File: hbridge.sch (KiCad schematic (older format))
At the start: 16 parts, among them M1 Motor_DC_ALT, Q1 VN2222L, Q2 VN2222L, Q3 IRFZ44, Q4 IRFZ44, Q5 IRFZ44, Q6 IRFZ44, U6 ILD74, U7 LT1161CN-PBF

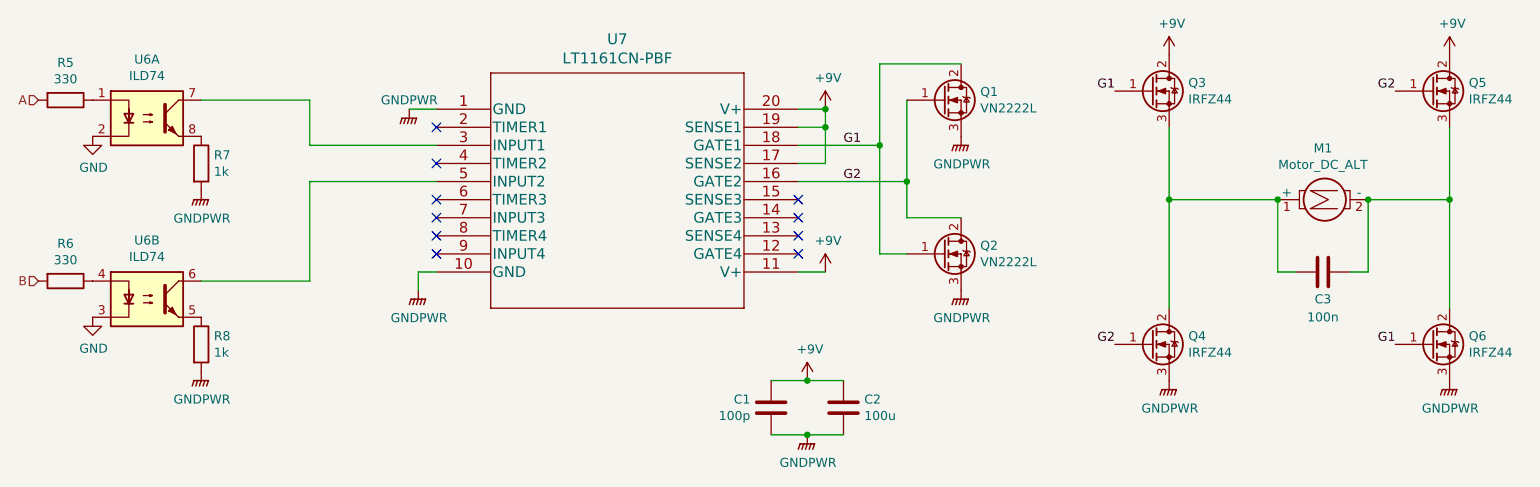
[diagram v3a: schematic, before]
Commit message: Add servos and can brush motor
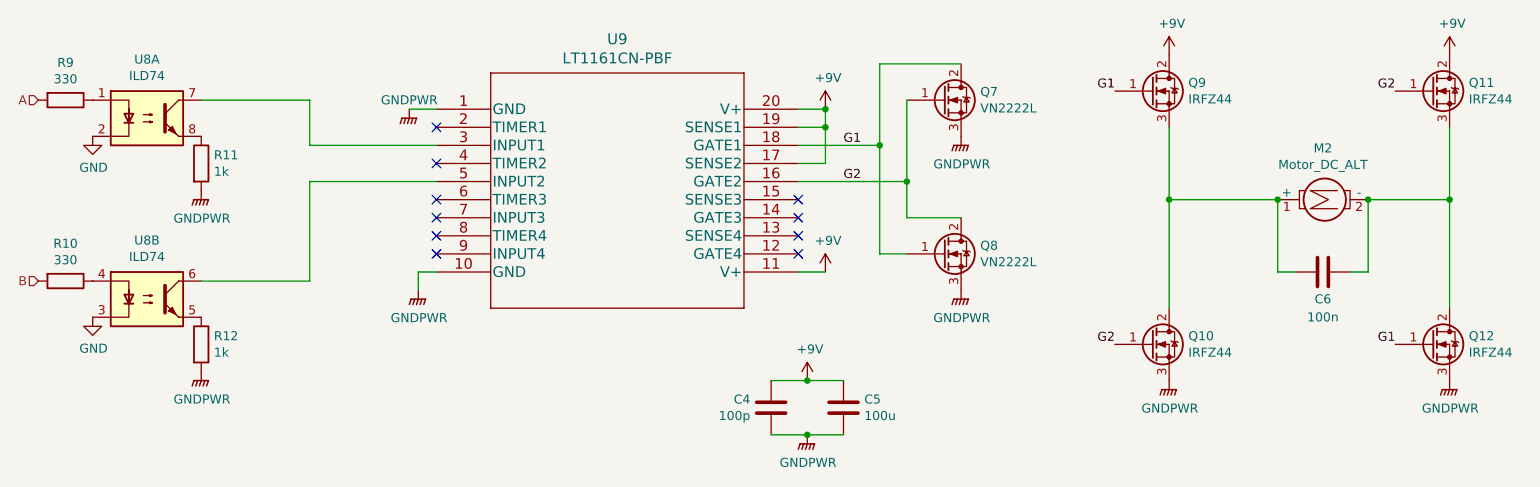
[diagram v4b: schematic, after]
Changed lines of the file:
@@
 AR Path="/5EFA9D4F/5EFAE763" Ref="M1"  Part="1"
 AR Path="/5F04487B/5EFAE763" Ref="M2"  Part="1"
-F 0 "M1" V 8716 3450 50  0000 C CNN
+F 0 "M2" V 8716 3450 50  0000 C CNN
 F 1 "Motor_DC_ALT" V 8807 3450 50  0000 C CNN
 F 2 "" H 9000 3410 50  0001 C CNN
@@
 AR Path="/5EFA9D4F/5EFB4C9B" Ref="U6"  Part="1"
 AR Path="/5F04487B/5EFB4C9B" Ref="U8"  Part="1"
-F 0 "U6" H 2550 3375 50  0000 C CNN
+F 0 "U8" H 2550 3375 50  0000 C CNN
 F 1 "ILD74" H 2550 3284 50  0000 C CNN
 F 2 "" H 2350 2850 50  0001 L CIN
@@
 AR Path="/5EFA9D4F/5EFB57BF" Ref="U6"  Part="2"
 AR Path="/5F04487B/5EFB57BF" Ref="U8"  Part="2"
-F 0 "U6" H 2550 4375 50  0000 C CNN
+F 0 "U8" H 2550 4375 50  0000 C CNN
 F 1 "ILD74" H 2550 4284 50  0000 C CNN
 F 2 "" H 2350 3850 50  0001 L CIN
@@
 AR Path="/5EFA9D4F/5EFB6EDB" Ref="R8"  Part="1"
 AR Path="/5F04487B/5EFB6EDB" Ref="R12"  Part="1"
-F 0 "R8" H 2920 4346 50  0000 L CNN
+F 0 "R12" H 2920 4346 50  0000 L CNN
 F 1 "1k" H 2920 4255 50  0000 L CNN
 F 2 "" V 2780 4300 50  0001 C CNN
@@
 AR Path="/5EFA9D4F/5EFB7506" Ref="R7"  Part="1"
 AR Path="/5F04487B/5EFB7506" Ref="R11"  Part="1"
-F 0 "R7" H 2920 3346 50  0000 L CNN
+F 0 "R11" H 2920 3346 50  0000 L CNN
 F 1 "1k" H 2920 3255 50  0000 L CNN
 F 2 "" V 2780 3300 50  0001 C CNN
@@
 AR Path="/5EFA9D4F/5EFB9D51" Ref="R5"  Part="1"
 AR Path="/5F04487B/5EFB9D51" Ref="R9"  Part="1"
-F 0 "R5" V 1893 2950 50  0000 C CNN
+F 0 "R9" V 1893 2950 50  0000 C CNN
 F 1 "330" V 1984 2950 50  0000 C CNN
 F 2 "" V 2030 2950 50  0001 C CNN
@@
 AR Path="/5EFA9D4F/5EFBA4CA" Ref="R6"  Part="1"
 AR Path="/5F04487B/5EFBA4CA" Ref="R10"  Part="1"
-F 0 "R6" V 1893 3950 50  0000 C CNN
+F 0 "R10" V 1893 3950 50  0000 C CNN
 F 1 "330" V 1984 3950 50  0000 C CNN
 F 2 "" V 2030 3950 50  0001 C CNN
@@
 AR Path="/5EFA9D4F/5EFBBB55" Ref="C1"  Part="1"
 AR Path="/5F04487B/5EFBBB55" Ref="C4"  Part="1"
-F 0 "C1" H 5885 4604 50  0000 R CNN
+F 0 "C4" H 5885 4604 50  0000 R CNN
 F 1 "100p" H 5885 4695 50  0000 R CNN
 F 2 "" H 6038 4500 50  0001 C CNN
@@
 AR Path="/5EFA9D4F/5EFBC147" Ref="C2"  Part="1"
 AR Path="/5F04487B/5EFBC147" Ref="C5"  Part="1"
-F 0 "C2" H 6515 4696 50  0000 L CNN
+F 0 "C5" H 6515 4696 50  0000 L CNN
 F 1 "100u" H 6515 4605 50  0000 L CNN
 F 2 "" H 6438 4500 50  0001 C CNN
@@
 AR Path="/5EFA9D4F/5EFE7548" Ref="Q1"  Part="1"
 AR Path="/5F04487B/5EFE7548" Ref="Q7"  Part="1"
-F 0 "Q1" H 7156 2996 50  0000 L CNN
+F 0 "Q7" H 7156 2996 50  0000 L CNN
 F 1 "VN2222L" H 7156 2905 50  0000 L CNN
 F 2 "" H 7150 3050 50  0001 C CNN
@@
 AR Path="/5EFA9D4F/5EFE9639" Ref="Q2"  Part="1"
 AR Path="/5F04487B/5EFE9639" Ref="Q8"  Part="1"
-F 0 "Q2" H 7156 3846 50  0000 L CNN
+F 0 "Q8" H 7156 3846 50  0000 L CNN
 F 1 "VN2222L" H 7156 3755 50  0000 L CNN
 F 2 "" H 7150 3900 50  0001 C CNN
@@
 AR Path="/5EFA9D4F/5EFE9DB0" Ref="Q3"  Part="1"
 AR Path="/5F04487B/5EFE9DB0" Ref="Q9"  Part="1"
-F 0 "Q3" H 8306 2946 50  0000 L CNN
+F 0 "Q9" H 8306 2946 50  0000 L CNN
 F 1 "IRFZ44" H 8306 2855 50  0000 L CNN
 F 2 "" H 8300 3000 50  0001 C CNN
@@
 AR Path="/5EFA9D4F/5EFEA31E" Ref="Q4"  Part="1"
 AR Path="/5F04487B/5EFEA31E" Ref="Q10"  Part="1"
-F 0 "Q4" H 8306 4346 50  0000 L CNN
+F 0 "Q10" H 8306 4346 50  0000 L CNN
 F 1 "IRFZ44" H 8306 4255 50  0000 L CNN
 F 2 "" H 8300 4400 50  0001 C CNN
@@
 AR Path="/5EFA9D4F/5EFEB4E2" Ref="Q5"  Part="1"
 AR Path="/5F04487B/5EFEB4E2" Ref="Q11"  Part="1"
-F 0 "Q5" H 9856 2946 50  0000 L CNN
+F 0 "Q11" H 9856 2946 50  0000 L CNN
 F 1 "IRFZ44" H 9856 2855 50  0000 L CNN
 F 2 "" H 9850 3000 50  0001 C CNN
@@
 AR Path="/5EFA9D4F/5EFEB900" Ref="Q6"  Part="1"
 AR Path="/5F04487B/5EFEB900" Ref="Q12"  Part="1"
-F 0 "Q6" H 9856 4346 50  0000 L CNN
+F 0 "Q12" H 9856 4346 50  0000 L CNN
 F 1 "IRFZ44" H 9856 4255 50  0000 L CNN
 F 2 "" H 9850 4400 50  0001 C CNN
@@
 AR Path="/5EFA9D4F/5EFAF223" Ref="C3"  Part="1"
 AR Path="/5F04487B/5EFAF223" Ref="C6"  Part="1"
-F 0 "C3" V 9200 3900 50  0000 C CNN
+F 0 "C6" V 9200 3900 50  0000 C CNN
 F 1 "100n" V 9300 3900 50  0000 C CNN
 F 2 "" H 9088 3750 50  0001 C CNN
@@
 AR Path="/5EFA9D4F/5EFCF468" Ref="U7"  Part="1"
 AR Path="/5F04487B/5EFCF468" Ref="U9"  Part="1"
-F 0 "U7" H 5150 3387 60  0000 C CNN
+F 0 "U9" H 5150 3387 60  0000 C CNN
 F 1 "LT1161CN-PBF" H 5150 3281 60  0000 C CNN
 F 2 "PDIP-20_N_LIT" H 5150 3240 60  0001 C CNN

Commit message: Misc minor fixes
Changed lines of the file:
@@
 $Descr A4 11693 8268
 encoding utf-8
-Sheet 2 6
+Sheet 3 6
 Title ""
 Date ""
@@
 AR Path="/5EFA9D4F/5EFAE763" Ref="M1"  Part="1"
 AR Path="/5F04487B/5EFAE763" Ref="M2"  Part="1"
-F 0 "M2" V 8716 3450 50  0000 C CNN
+F 0 "M1" V 8716 3450 50  0000 C CNN
 F 1 "Motor_DC_ALT" V 8807 3450 50  0000 C CNN
 F 2 "" H 9000 3410 50  0001 C CNN
@@
 AR Path="/5EFA9D4F/5EFB4C9B" Ref="U6"  Part="1"
 AR Path="/5F04487B/5EFB4C9B" Ref="U8"  Part="1"
-F 0 "U8" H 2550 3375 50  0000 C CNN
+F 0 "U6" H 2550 3375 50  0000 C CNN
 F 1 "ILD74" H 2550 3284 50  0000 C CNN
 F 2 "" H 2350 2850 50  0001 L CIN
@@
 AR Path="/5EFA9D4F/5EFB57BF" Ref="U6"  Part="2"
 AR Path="/5F04487B/5EFB57BF" Ref="U8"  Part="2"
-F 0 "U8" H 2550 4375 50  0000 C CNN
+F 0 "U6" H 2550 4375 50  0000 C CNN
 F 1 "ILD74" H 2550 4284 50  0000 C CNN
 F 2 "" H 2350 3850 50  0001 L CIN
@@
 AR Path="/5EFA9D4F/5EFB6EDB" Ref="R8"  Part="1"
 AR Path="/5F04487B/5EFB6EDB" Ref="R12"  Part="1"
-F 0 "R12" H 2920 4346 50  0000 L CNN
+F 0 "R8" H 2920 4346 50  0000 L CNN
 F 1 "1k" H 2920 4255 50  0000 L CNN
 F 2 "" V 2780 4300 50  0001 C CNN
@@
 AR Path="/5EFA9D4F/5EFB7506" Ref="R7"  Part="1"
 AR Path="/5F04487B/5EFB7506" Ref="R11"  Part="1"
-F 0 "R11" H 2920 3346 50  0000 L CNN
+F 0 "R7" H 2920 3346 50  0000 L CNN
 F 1 "1k" H 2920 3255 50  0000 L CNN
 F 2 "" V 2780 3300 50  0001 C CNN
@@
 AR Path="/5EFA9D4F/5EFB9D51" Ref="R5"  Part="1"
 AR Path="/5F04487B/5EFB9D51" Ref="R9"  Part="1"
-F 0 "R9" V 1893 2950 50  0000 C CNN
+F 0 "R5" V 1893 2950 50  0000 C CNN
 F 1 "330" V 1984 2950 50  0000 C CNN
 F 2 "" V 2030 2950 50  0001 C CNN
@@
 AR Path="/5EFA9D4F/5EFBA4CA" Ref="R6"  Part="1"
 AR Path="/5F04487B/5EFBA4CA" Ref="R10"  Part="1"
-F 0 "R10" V 1893 3950 50  0000 C CNN
+F 0 "R6" V 1893 3950 50  0000 C CNN
 F 1 "330" V 1984 3950 50  0000 C CNN
 F 2 "" V 2030 3950 50  0001 C CNN
@@
 AR Path="/5EFA9D4F/5EFBBB55" Ref="C1"  Part="1"
 AR Path="/5F04487B/5EFBBB55" Ref="C4"  Part="1"
-F 0 "C4" H 5885 4604 50  0000 R CNN
+F 0 "C1" H 5885 4604 50  0000 R CNN
 F 1 "100p" H 5885 4695 50  0000 R CNN
 F 2 "" H 6038 4500 50  0001 C CNN
@@
 AR Path="/5EFA9D4F/5EFBC147" Ref="C2"  Part="1"
 AR Path="/5F04487B/5EFBC147" Ref="C5"  Part="1"
-F 0 "C5" H 6515 4696 50  0000 L CNN
+F 0 "C2" H 6515 4696 50  0000 L CNN
 F 1 "100u" H 6515 4605 50  0000 L CNN
 F 2 "" H 6438 4500 50  0001 C CNN
@@
 AR Path="/5EFA9D4F/5EFE7548" Ref="Q1"  Part="1"
 AR Path="/5F04487B/5EFE7548" Ref="Q7"  Part="1"
-F 0 "Q7" H 7156 2996 50  0000 L CNN
+F 0 "Q1" H 7156 2996 50  0000 L CNN
 F 1 "VN2222L" H 7156 2905 50  0000 L CNN
 F 2 "" H 7150 3050 50  0001 C CNN
@@
 AR Path="/5EFA9D4F/5EFE9639" Ref="Q2"  Part="1"
 AR Path="/5F04487B/5EFE9639" Ref="Q8"  Part="1"
-F 0 "Q8" H 7156 3846 50  0000 L CNN
+F 0 "Q2" H 7156 3846 50  0000 L CNN
 F 1 "VN2222L" H 7156 3755 50  0000 L CNN
 F 2 "" H 7150 3900 50  0001 C CNN
@@
 AR Path="/5EFA9D4F/5EFE9DB0" Ref="Q3"  Part="1"
 AR Path="/5F04487B/5EFE9DB0" Ref="Q9"  Part="1"
-F 0 "Q9" H 8306 2946 50  0000 L CNN
+F 0 "Q3" H 8306 2946 50  0000 L CNN
 F 1 "IRFZ44" H 8306 2855 50  0000 L CNN
 F 2 "" H 8300 3000 50  0001 C CNN
@@
 AR Path="/5EFA9D4F/5EFEA31E" Ref="Q4"  Part="1"
 AR Path="/5F04487B/5EFEA31E" Ref="Q10"  Part="1"
-F 0 "Q10" H 8306 4346 50  0000 L CNN
+F 0 "Q4" H 8306 4346 50  0000 L CNN
 F 1 "IRFZ44" H 8306 4255 50  0000 L CNN
 F 2 "" H 8300 4400 50  0001 C CNN
@@
 AR Path="/5EFA9D4F/5EFEB4E2" Ref="Q5"  Part="1"
 AR Path="/5F04487B/5EFEB4E2" Ref="Q11"  Part="1"
-F 0 "Q11" H 9856 2946 50  0000 L CNN
+F 0 "Q5" H 9856 2946 50  0000 L CNN
 F 1 "IRFZ44" H 9856 2855 50  0000 L CNN
 F 2 "" H 9850 3000 50  0001 C CNN
@@
 AR Path="/5EFA9D4F/5EFEB900" Ref="Q6"  Part="1"
 AR Path="/5F04487B/5EFEB900" Ref="Q12"  Part="1"
-F 0 "Q12" H 9856 4346 50  0000 L CNN
+F 0 "Q6" H 9856 4346 50  0000 L CNN
 F 1 "IRFZ44" H 9856 4255 50  0000 L CNN
 F 2 "" H 9850 4400 50  0001 C CNN
@@
 AR Path="/5EFA9D4F/5EFAF223" Ref="C3"  Part="1"
 AR Path="/5F04487B/5EFAF223" Ref="C6"  Part="1"
-F 0 "C6" V 9200 3900 50  0000 C CNN
+F 0 "C3" V 9200 3900 50  0000 C CNN
 F 1 "100n" V 9300 3900 50  0000 C CNN
 F 2 "" H 9088 3750 50  0001 C CNN
@@
 AR Path="/5EFA9D4F/5EFCF468" Ref="U7"  Part="1"
 AR Path="/5F04487B/5EFCF468" Ref="U9"  Part="1"
-F 0 "U9" H 5150 3387 60  0000 C CNN
+F 0 "U7" H 5150 3387 60  0000 C CNN
 F 1 "LT1161CN-PBF" H 5150 3281 60  0000 C CNN
 F 2 "PDIP-20_N_LIT" H 5150 3240 60  0001 C CNN
